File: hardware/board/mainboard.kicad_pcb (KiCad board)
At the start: 4 copper layers, 60 x 110 mm, 266 parts, among them J201 Power, Q601 BCM847, Q701 BCM847, Q801 BCM847, U1 TL074, U2 TL074, U201 TL431A, U3 TL074, U4 TL074, U5 TL074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

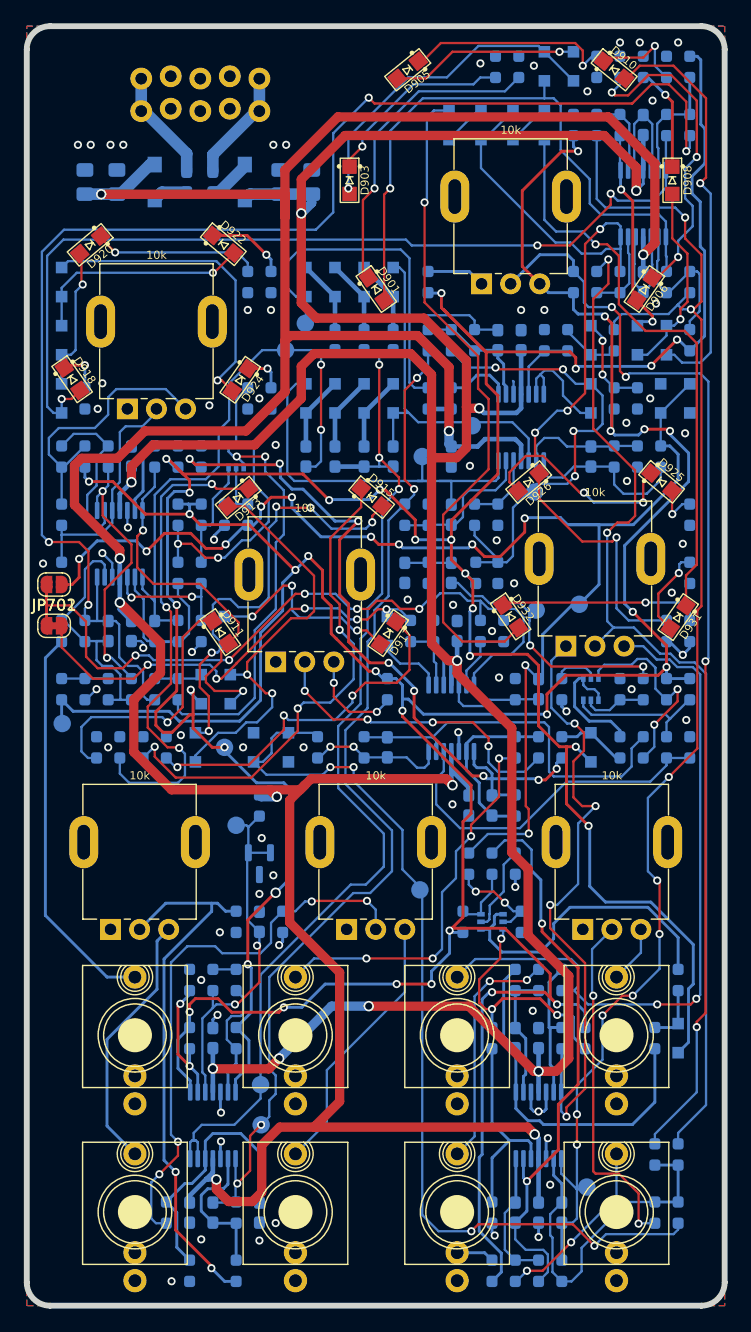
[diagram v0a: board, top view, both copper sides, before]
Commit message: Moved +-12v to internal layer, cleaned up silkscreen
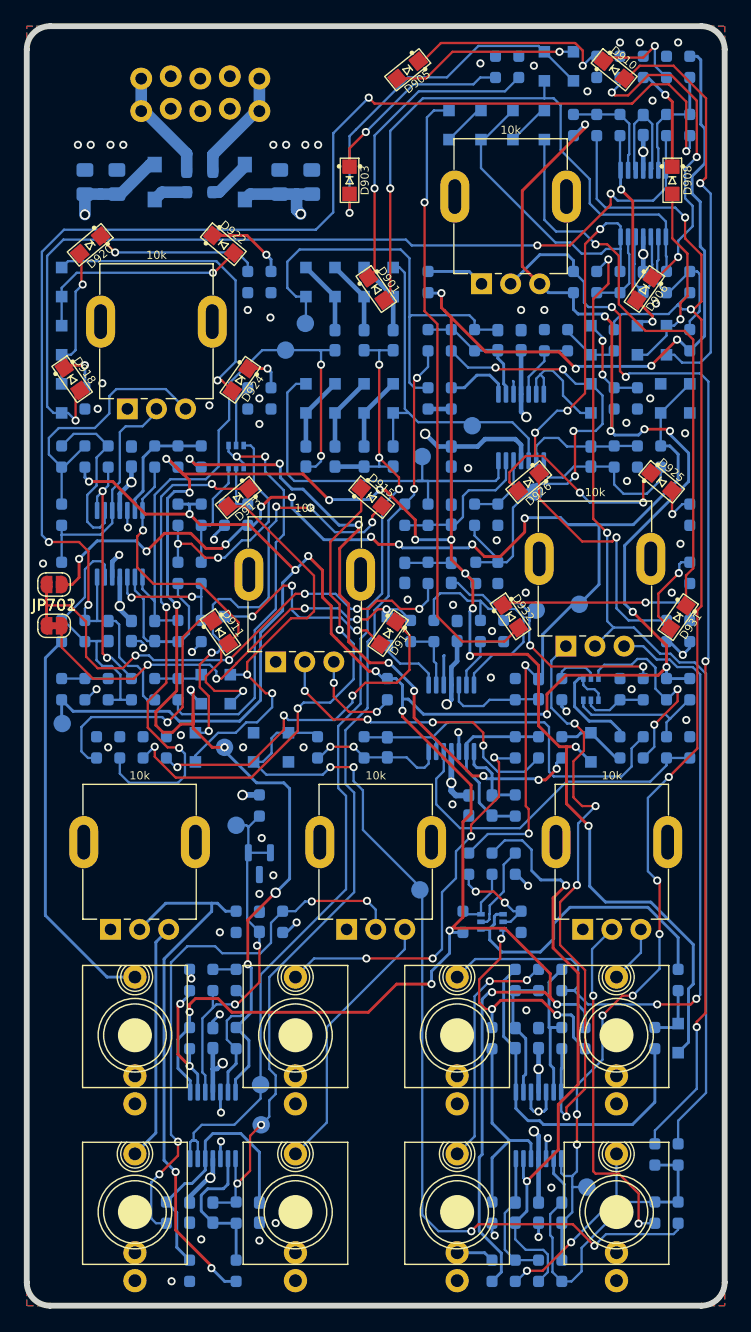
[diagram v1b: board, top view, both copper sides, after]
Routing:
- net +12V: track 288.9 -> 263.7 mm, vias 9 -> 8
- net -12V: track 243.3 -> 230.9 mm, vias 9 -> 7
- net /Filter Core/LOW_PASS_IN: track 89.4 -> 85.2 mm
- net -8VREF: track 246.7 -> 242.7 mm
- net Net-(D902-K): track 28.2 -> 31.9 mm
- net /Filter Core/HIGH_PASS_IN: track 93.5 -> 90.0 mm
- net Net-(D930-K): track 57.2 -> 53.9 mm
- net /Cutoff CV Driver/FM1_OUT: track 90.1 -> 87.6 mm
- net Net-(J301-Tip): track 22.5 -> 20.5 mm
- net Net-(U2B--): track 49.6 -> 51.6 mm
- net /Resonance VCA/Resonance_Potentiometer: track 23.3 -> 21.4 mm
- net +8VREF: track 281.8 -> 283.5 mm, vias 21 -> 19
- net Net-(D918-A): track 79.0 -> 80.2 mm
- net Net-(R404-Pad1): track 54.3 -> 53.2 mm
- net /Cutoff CV Driver/CUTOFF_OUT: track 125.0 -> 124.1 mm
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
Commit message: Some minor routing improvements
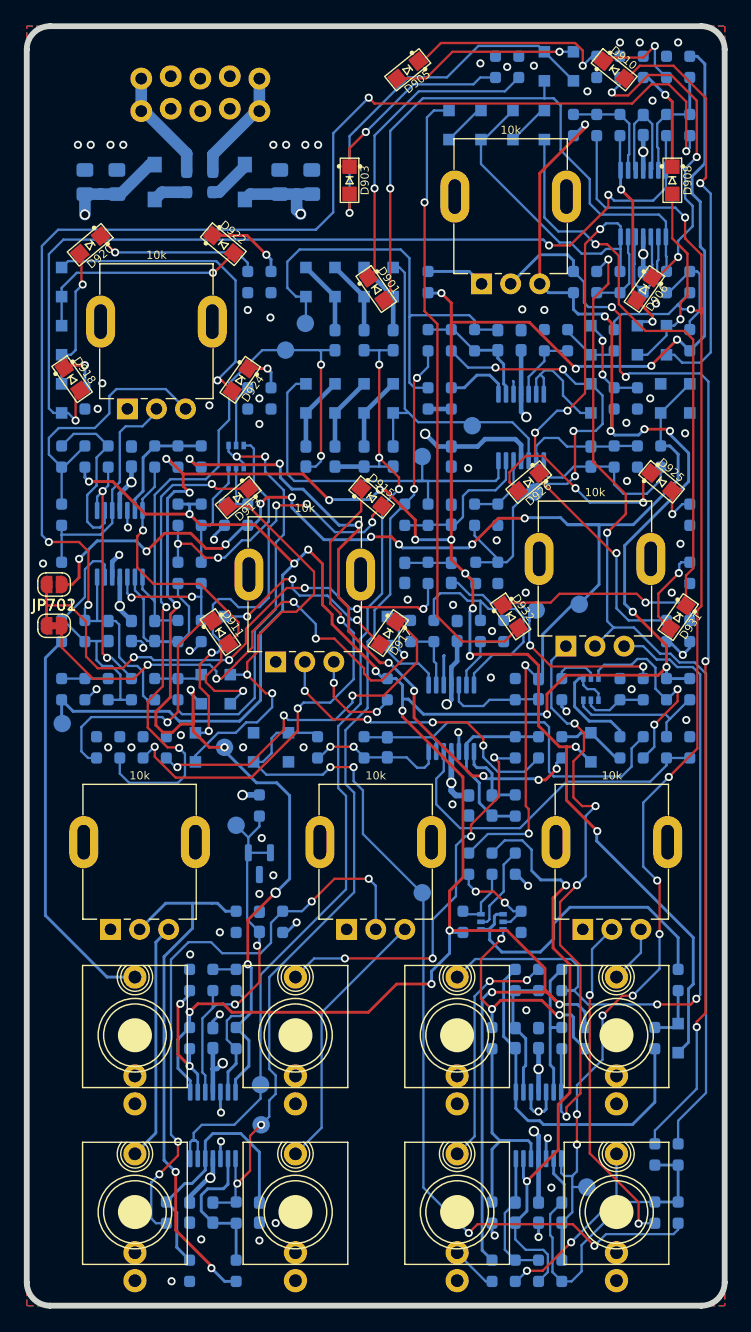
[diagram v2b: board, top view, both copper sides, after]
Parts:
- moved TP702 0.32 mm to (84.7, 124.8)
- turned R801 to 90 degrees
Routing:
- net Net-(D701-K): track 39.7 -> 47.3 mm
- net +8VREF: track 283.5 -> 278.5 mm
- net -8VREF: track 242.7 -> 238.7 mm
- net Net-(R304-Pad1): track 48.0 -> 51.2 mm
- net Net-(D926-K): track 21.3 -> 19.3 mm
- net /Filter Core/OUT: track 116.6 -> 115.2 mm
- net /Cutoff CV Driver/FM1_OUT: track 87.6 -> 88.9 mm
- net /Cutoff CV Driver/INSTABILITY_IN: track 81.9 -> 80.6 mm
- net Net-(R407-Pad2): track 30.2 -> 29.2 mm
- net Net-(U2B-+): track 17.7 -> 18.6 mm
- net /Cutoff CV Driver/CUTOFF_OUT: track 124.1 -> 125.0 mm
- net Net-(JP701-B): track 46.2 -> 47.0 mm
- net Net-(J801-Tip_normalize): track 3.26 -> 4.02 mm
- net Net-(D917-K): track 30.7 -> 31.4 mm
- net Net-(R301-Pad1): track 46.9 -> 46.2 mm
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
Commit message: More minor changes
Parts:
- moved R807 5.00 mm to (88.2, 127.2)
- moved R809 5.00 mm to (93.2, 127.2)
- moved R808 2.00 mm to (90.7, 122.2), turned to -90 degrees
- moved R811 2.00 mm to (92.7, 122.2)
- turned Q801 to 90 degrees
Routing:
- net Net-(Q801-B-Pad5): track 7.44 -> 3.14 mm
- net Net-(U2B--): track 51.0 -> 47.0 mm
- net +8VREF: track 278.5 -> 275.3 mm, vias 19 -> 18
- net GND: track 55.4 -> 53.8 mm, vias 77 -> 78
- net Net-(Q801-E-Pad1): track 27.2 -> 25.6 mm
- net Net-(Q801-B-Pad2): track 8.26 -> 6.95 mm, vias 2 -> 0
- net /Filter Core/OUT: track 115.2 -> 116.2 mm
- net Net-(Q801-C-Pad3): track 20.7 -> 19.7 mm
- net /Cutoff CV Driver/INSTABILITY_IN: track 80.6 -> 79.8 mm
- net -12V: track 230.9 -> 230.1 mm
- net -8VREF: track 238.7 -> 239.4 mm
- net Net-(D914-K): track 39.3 -> 39.9 mm
